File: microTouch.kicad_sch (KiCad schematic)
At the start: 9 parts, among them J1 SERVO, J2 PRINTER, U1 T1302

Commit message: smaller
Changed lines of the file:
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@@
   )
   (symbol (lib_id "Device:LED") (at 105.41 82.55 180) (unit 1)
-    (in_bom yes) (on_board yes) (fields_autoplaced)
-    (property "Reference" "D1" (id 0) (at 105.7909 76.4245 0))
-    (property "Value" "LED" (id 1) (at 105.7909 79.1996 0))
+    (in_bom yes) (on_board yes)
+    (property "Reference" "D1" (id 0) (at 105.7909 85.3145 0))
+    (property "Value" "LED" (id 1) (at 105.7909 88.0896 0))
     (property "Footprint" "LED_SMD:LED_0603_1608Metric_Pad1.05x0.95mm_HandSolder" (id 2) (at 105.41 82.55 0)
       (effects (font (size 1.27 1.27)) hide)

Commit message: assorted tweaks
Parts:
- D1: footprint LED_SMD:LED_0603_1608Metric_Pad1.05x0.95mm_HandSolder -> LED_SMD:LED_0805_2012Metric_Pad1.15x1.40mm_HandSolder
- R1, R2, R3: footprint Resistor_SMD:R_0603_1608Metric_Pad0.98x0.95mm_HandSolder -> Resistor_SMD:R_0805_2012Metric_Pad1.20x1.40mm_HandSolder
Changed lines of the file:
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@@
     (property "Reference" "R1" (id 0) (at 86.36 58.7969 90))
     (property "Value" "220" (id 1) (at 86.36 61.572 90))
-    (property "Footprint" "Resistor_SMD:R_0603_1608Metric_Pad0.98x0.95mm_HandSolder" (id 2) (at 86.36 63.5 0)
+    (property "Footprint" "Resistor_SMD:R_0805_2012Metric_Pad1.20x1.40mm_HandSolder" (id 2) (at 86.36 63.5 0)
       (effects (font (size 1.27 1.27)) hide)
     )
@@
     (property "Reference" "R2" (id 0) (at 105.41 68.9569 90))
     (property "Value" "1K" (id 1) (at 105.41 71.732 90))
-    (property "Footprint" "Resistor_SMD:R_0603_1608Metric_Pad0.98x0.95mm_HandSolder" (id 2) (at 105.41 73.66 0)
+    (property "Footprint" "Resistor_SMD:R_0805_2012Metric_Pad1.20x1.40mm_HandSolder" (id 2) (at 105.41 73.66 0)
       (effects (font (size 1.27 1.27)) hide)
     )
@@
     (property "Reference" "R3" (id 0) (at 114.3 77.8469 90))
     (property "Value" "2K2" (id 1) (at 114.3 80.622 90))
-    (property "Footprint" "Resistor_SMD:R_0603_1608Metric_Pad0.98x0.95mm_HandSolder" (id 2) (at 114.3 82.55 0)
+    (property "Footprint" "Resistor_SMD:R_0805_2012Metric_Pad1.20x1.40mm_HandSolder" (id 2) (at 114.3 82.55 0)
       (effects (font (size 1.27 1.27)) hide)
     )
@@
     (property "Reference" "D1" (id 0) (at 105.7909 85.3145 0))
     (property "Value" "LED" (id 1) (at 105.7909 88.0896 0))
-    (property "Footprint" "LED_SMD:LED_0603_1608Metric_Pad1.05x0.95mm_HandSolder" (id 2) (at 105.41 82.55 0)
+    (property "Footprint" "LED_SMD:LED_0805_2012Metric_Pad1.15x1.40mm_HandSolder" (id 2) (at 105.41 82.55 0)
       (effects (font (size 1.27 1.27)) hide)
     )
@@
     )
     (path "/7408d9bb-2040-4db4-9f32-e25e485fbe0e"
-      (reference "D1") (unit 1) (value "LED") (footprint "LED_SMD:LED_0603_1608Metric_Pad1.05x0.95mm_HandSolder")
+      (reference "D1") (unit 1) (value "LED") (footprint "LED_SMD:LED_0805_2012Metric_Pad1.15x1.40mm_HandSolder")
     )
     (path "/0c5ed85d-1f3f-4d6f-ab20-e65b16190c7b"
@@
     )
     (path "/addec1fb-b8e8-4fc7-8f03-f3f97a48f7fe"
-      (reference "R1") (unit 1) (value "220") (footprint "Resistor_SMD:R_0603_1608Metric_Pad0.98x0.95mm_HandSolder")
+      (reference "R1") (unit 1) (value "220") (footprint "Resistor_SMD:R_0805_2012Metric_Pad1.20x1.40mm_HandSolder")
     )
     (path "/d6cfadea-d8b7-4535-b6c3-a7d2fdbcf92b"
-      (reference "R2") (unit 1) (value "1K") (footprint "Resistor_SMD:R_0603_1608Metric_Pad0.98x0.95mm_HandSolder")
+      (reference "R2") (unit 1) (value "1K") (footprint "Resistor_SMD:R_0805_2012Metric_Pad1.20x1.40mm_HandSolder")
     )
     (path "/6ec2e99d-5757-45f7-89ab-e4a3e466c2e0"
-      (reference "R3") (unit 1) (value "2K2") (footprint "Resistor_SMD:R_0603_1608Metric_Pad0.98x0.95mm_HandSolder")
+      (reference "R3") (unit 1) (value "2K2") (footprint "Resistor_SMD:R_0805_2012Metric_Pad1.20x1.40mm_HandSolder")
     )
     (path "/a4631f7f-c98e-425f-863a-b5265e18ace0"

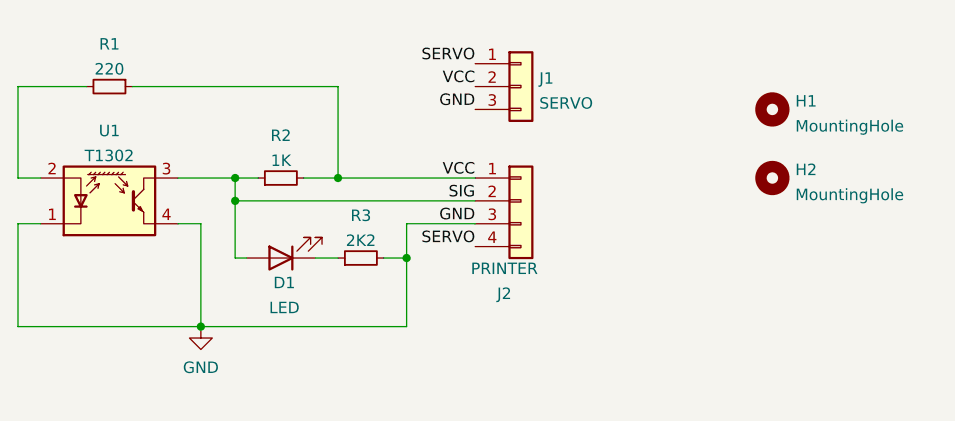
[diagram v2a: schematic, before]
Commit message: fix photint pinout, adjust pullup, move LED out further
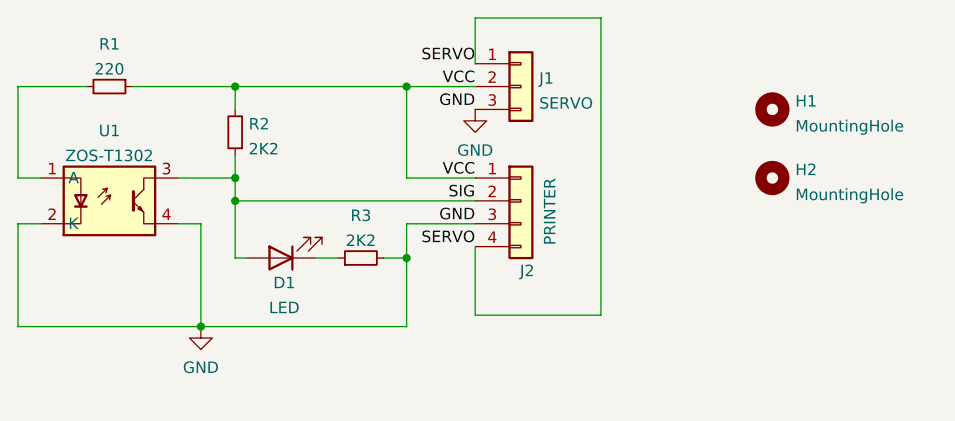
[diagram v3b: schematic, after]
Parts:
- removed U1: T1302, microTouch:T1302, symbol Sensor_Proximity:BPR-105F
- added U1: ZOS-T1302, microTouch:T1302, symbol microTouch:ZOS-T1302
- R2: value 1K -> 2K2
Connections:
- net GND: now also U1.2 (K), U1.4
- net SIG: now also U1.3
- net at R1.2: now also U1.1 (A)
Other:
- moved on the sheet: R2
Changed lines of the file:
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@@
   (paper "A4")
   (junction (at 96.52 90.17) (diameter 0) (color 0 0 0 0))
+  (junction (at 100.33 63.5) (diameter 0) (color 0 0 0 0))
   (junction (at 100.33 73.66) (diameter 0) (color 0 0 0 0))
   (junction (at 100.33 76.2) (diameter 0) (color 0 0 0 0))
-  (junction (at 111.76 73.66) (diameter 0) (color 0 0 0 0))
+  (junction (at 119.38 63.5) (diameter 0) (color 0 0 0 0))
   (junction (at 119.38 82.55) (diameter 0) (color 0 0 0 0))
   (wire (pts (xy 76.2 63.5) (xy 76.2 73.66))
@@
     (stroke (width 0) (type default) (color 0 0 0 0))
   )
-  (wire (pts (xy 88.9 63.5) (xy 111.76 63.5))
+  (wire (pts (xy 88.9 63.5) (xy 100.33 63.5))
     (stroke (width 0) (type default) (color 0 0 0 0))
   )
@@
     (stroke (width 0) (type default) (color 0 0 0 0))
   )
-  (wire (pts (xy 100.33 73.66) (xy 102.87 73.66))
+  (wire (pts (xy 100.33 63.5) (xy 100.33 66.04))
+    (stroke (width 0) (type default) (color 0 0 0 0))
+  )
+  (wire (pts (xy 100.33 63.5) (xy 119.38 63.5))
+    (stroke (width 0) (type default) (color 0 0 0 0))
+  )
+  (wire (pts (xy 100.33 71.12) (xy 100.33 73.66))
     (stroke (width 0) (type default) (color 0 0 0 0))
   )
@@
     (stroke (width 0) (type default) (color 0 0 0 0))
   )
-  (wire (pts (xy 107.95 73.66) (xy 111.76 73.66))
-    (stroke (width 0) (type default) (color 0 0 0 0))
-  )
   (wire (pts (xy 109.22 82.55) (xy 111.76 82.55))
     (stroke (width 0) (type default) (color 0 0 0 0))
   )
-  (wire (pts (xy 111.76 63.5) (xy 111.76 73.66))
-    (stroke (width 0) (type default) (color 0 0 0 0))
-  )
-  (wire (pts (xy 111.76 73.66) (xy 127 73.66))
-    (stroke (width 0) (type default) (color 0 0 0 0))
-  )
   (wire (pts (xy 116.84 82.55) (xy 119.38 82.55))
     (stroke (width 0) (type default) (color 0 0 0 0))
   )
+  (wire (pts (xy 119.38 63.5) (xy 127 63.5))
+    (stroke (width 0) (type default) (color 0 0 0 0))
+  )
+  (wire (pts (xy 119.38 73.66) (xy 119.38 63.5))
+    (stroke (width 0) (type default) (color 0 0 0 0))
+  )
   (wire (pts (xy 119.38 78.74) (xy 127 78.74))
     (stroke (width 0) (type default) (color 0 0 0 0))
@@
     (stroke (width 0) (type default) (color 0 0 0 0))
   )
+  (wire (pts (xy 127 55.88) (xy 140.97 55.88))
+    (stroke (width 0) (type default) (color 0 0 0 0))
+  )
+  (wire (pts (xy 127 60.96) (xy 127 55.88))
+    (stroke (width 0) (type default) (color 0 0 0 0))
+  )
+  (wire (pts (xy 127 73.66) (xy 119.38 73.66))
+    (stroke (width 0) (type default) (color 0 0 0 0))
+  )
   (wire (pts (xy 127 76.2) (xy 100.33 76.2))
+    (stroke (width 0) (type default) (color 0 0 0 0))
+  )
+  (wire (pts (xy 127 88.9) (xy 127 81.28))
+    (stroke (width 0) (type default) (color 0 0 0 0))
+  )
+  (wire (pts (xy 140.97 55.88) (xy 140.97 88.9))
+    (stroke (width 0) (type default) (color 0 0 0 0))
+  )
+  (wire (pts (xy 140.97 88.9) (xy 127 88.9))
     (stroke (width 0) (type default) (color 0 0 0 0))
   )
@@
     )
     (property "Datasheet" "" (id 3) (at 96.52 90.17 0)
+      (effects (font (size 1.27 1.27)) hide)
+    )
+    (pin "1")
+  )
+  (symbol (lib_id "power:GND") (at 127 66.04 0) (unit 1)
+    (in_bom yes) (on_board yes) (fields_autoplaced)
+    (property "Reference" "#PWR?" (id 0) (at 127 72.39 0)
+      (effects (font (size 1.27 1.27)) hide)
+    )
+    (property "Value" "GND" (id 1) (at 127 70.6024 0))
+    (property "Footprint" "" (id 2) (at 127 66.04 0)
+      (effects (font (size 1.27 1.27)) hide)
+    )
+    (property "Datasheet" "" (id 3) (at 127 66.04 0)
       (effects (font (size 1.27 1.27)) hide)
     )
@@
     (pin "2")
   )
-  (symbol (lib_id "Device:R_Small") (at 105.41 73.66 90) (unit 1)
-    (in_bom yes) (on_board yes) (fields_autoplaced)
-    (property "Reference" "R2" (id 0) (at 105.41 68.9569 90))
-    (property "Value" "1K" (id 1) (at 105.41 71.732 90))
-    (property "Footprint" "Resistor_SMD:R_0805_2012Metric_Pad1.20x1.40mm_HandSolder" (id 2) (at 105.41 73.66 0)
-      (effects (font (size 1.27 1.27)) hide)
-    )
-    (property "Datasheet" "~" (id 3) (at 105.41 73.66 0)
+  (symbol (lib_id "Device:R_Small") (at 100.33 68.58 180) (unit 1)
+    (in_bom yes) (on_board yes) (fields_autoplaced)
+    (property "Reference" "R2" (id 0) (at 101.8286 67.6715 0)
+      (effects (font (size 1.27 1.27)) (justify right))
+    )
+    (property "Value" "2K2" (id 1) (at 101.8286 70.4466 0)
+      (effects (font (size 1.27 1.27)) (justify right))
+    )
+    (property "Footprint" "Resistor_SMD:R_0805_2012Metric_Pad1.20x1.40mm_HandSolder" (id 2) (at 100.33 68.58 0)
+      (effects (font (size 1.27 1.27)) hide)
+    )
+    (property "Datasheet" "~" (id 3) (at 100.33 68.58 0)
       (effects (font (size 1.27 1.27)) hide)
     )
@@
   )
   (symbol (lib_id "Connector_Generic:Conn_01x04") (at 132.08 76.2 0) (unit 1)
-    (in_bom yes) (on_board yes) (fields_autoplaced)
-    (property "Reference" "J2" (id 0) (at 130.2385 86.5165 0))
-    (property "Value" "PRINTER" (id 1) (at 130.2385 83.7414 0))
+    (in_bom yes) (on_board yes)
+    (property "Reference" "J2" (id 0) (at 132.7785 83.9765 0))
+    (property "Value" "PRINTER" (id 1) (at 135.3185 77.3914 90))
     (property "Footprint" "Connector_JST:JST_PH_B4B-PH-K_1x04_P2.00mm_Vertical" (id 2) (at 132.08 76.2 0)
       (effects (font (size 1.27 1.27)) hide)
@@
     (pin "4")
   )
-  (symbol (lib_id "Sensor_Proximity:BPR-105F") (at 86.36 76.2 0) (unit 1)
+  (symbol (lib_id "microTouch:ZOS-T1302") (at 86.36 76.2 0) (unit 1)
     (in_bom yes) (on_board yes) (fields_autoplaced)
     (property "Reference" "U1" (id 0) (at 86.36 68.4235 0))
-    (property "Value" "T1302" (id 1) (at 86.36 71.1986 0))
-    (property "Footprint" "microTouch:T1302" (id 2) (at 86.36 81.28 0)
-      (effects (font (size 1.27 1.27)) hide)
-    )
-    (property "Datasheet" "http://www.ystone.com.tw/en/data/goods/IRPT/Photo%20Interrupters-Reflective%20Type.pdf" (id 3) (at 86.36 73.66 0)
+    (property "Value" "ZOS-T1302" (id 1) (at 86.36 71.1986 0))
+    (property "Footprint" "microTouch:T1302" (id 2) (at 86.36 76.2 0)
+      (effects (font (size 1.27 1.27)) hide)
+    )
+    (property "Datasheet" "" (id 3) (at 86.36 76.2 0)
       (effects (font (size 1.27 1.27)) hide)
     )
@@
       (reference "#PWR01") (unit 1) (value "GND") (footprint "")
     )
+    (path "/615251e4-00d3-4694-93b4-edb937059fda"
+      (reference "#PWR?") (unit 1) (value "GND") (footprint "")
+    )
     (path "/7408d9bb-2040-4db4-9f32-e25e485fbe0e"
       (reference "D1") (unit 1) (value "LED") (footprint "LED_SMD:LED_0805_2012Metric_Pad1.15x1.40mm_HandSolder")
@@
     )
     (path "/d6cfadea-d8b7-4535-b6c3-a7d2fdbcf92b"
-      (reference "R2") (unit 1) (value "1K") (footprint "Resistor_SMD:R_0805_2012Metric_Pad1.20x1.40mm_HandSolder")
+      (reference "R2") (unit 1) (value "2K2") (footprint "Resistor_SMD:R_0805_2012Metric_Pad1.20x1.40mm_HandSolder")
     )
     (path "/6ec2e99d-5757-45f7-89ab-e4a3e466c2e0"
       (reference "R3") (unit 1) (value "2K2") (footprint "Resistor_SMD:R_0805_2012Metric_Pad1.20x1.40mm_HandSolder")
     )
-    (path "/a4631f7f-c98e-425f-863a-b5265e18ace0"
-      (reference "U1") (unit 1) (value "T1302") (footprint "microTouch:T1302")
-    )
-  )
+    (path "/5c366571-0b2a-4b91-b149-dcee62dd11ce"
+      (reference "U1") (unit 1) (value "ZOS-T1302") (footprint "microTouch:T1302")
+    )
+  )

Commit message: redesign with a A3144 hall effect sensor
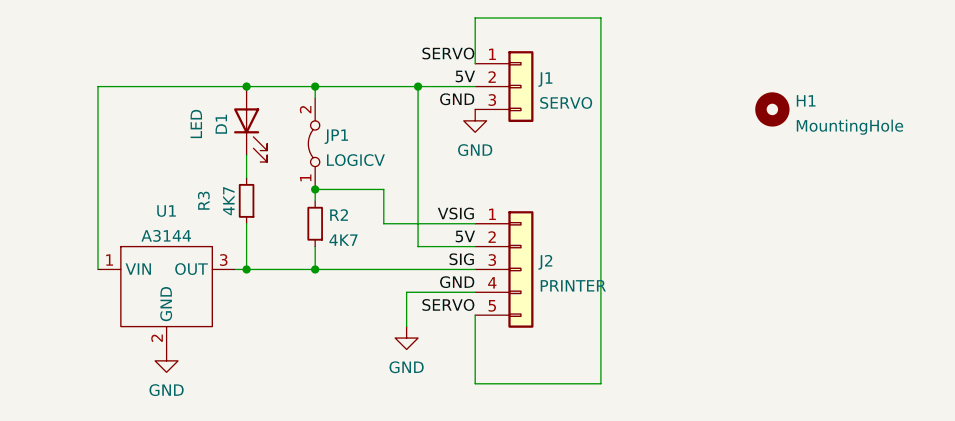
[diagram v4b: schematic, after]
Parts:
- removed H2: MountingHole, MountingHole:MountingHole_3.2mm_M3, symbol Mechanical:MountingHole
- removed J2: PRINTER, Connector_JST:JST_PH_B4B-PH-K_1x04_P2.00mm_Vertical, symbol Connector_Generic:Conn_01x04
- removed R1: 220, Resistor_SMD:R_0805_2012Metric_Pad1.20x1.40mm_HandSolder, symbol Device:R_Small
- removed U1: ZOS-T1302, microTouch:T1302, symbol microTouch:ZOS-T1302
- added J2: PRINTER, Connector_JST:JST_PH_B5B-PH-K_1x05_P2.00mm_Vertical, symbol Connector_Generic:Conn_01x05
- added JP1: LOGICV, Jumper:SolderJumper-2_P1.3mm_Bridged_RoundedPad1.0x1.5mm, symbol Jumper:Jumper_2_Bridged
- added U1: A3144, Package_TO_SOT_THT:TO-92Flat, symbol microTouch:A3144
- R2, R3: value 2K2 -> 4K7
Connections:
- net GND: now also J2.4 (Pin_4), U1.2 (GND); no longer R3.2
- net SERVO: now also J2.5 (Pin_5)
- net SIG: now also R3.1, J2.3 (Pin_3), U1.3 (OUT); no longer D1.2 (A)
- net at D1.1 (K): now also R3.2; no longer R3.1
- net VCC renamed 5V
- net 5V: now also D1.2 (A), J2.2 (Pin_2), JP1.2 (B), U1.1 (VIN); no longer R2.2
- new net VSIG: J2.1 (Pin_1), JP1.1 (A), R2.2
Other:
- moved on the sheet: D1, R2, R3

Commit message: move some stuff around, add some filter caps for noise
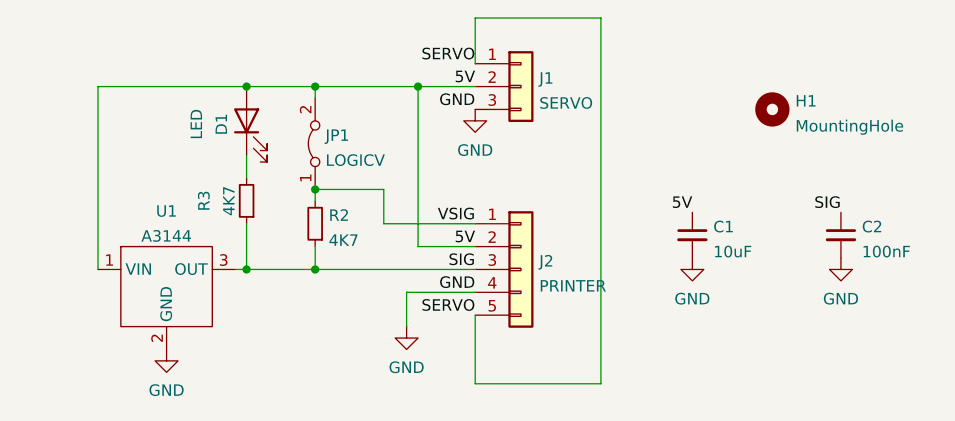
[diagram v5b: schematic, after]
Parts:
- added C1: 10uF, Capacitor_SMD:C_0805_2012Metric_Pad1.18x1.45mm_HandSolder, symbol Device:C_Small
- added C2: 100nF, Capacitor_SMD:C_0805_2012Metric_Pad1.18x1.45mm_HandSolder, symbol Device:C_Small
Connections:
- net 5V: now also C1.1
- net GND: now also C1.2, C2.2
- net SIG: now also C2.1
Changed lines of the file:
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@@
+    (effects (font (size 1.27 1.27)) (justify right bottom))
+  )
+  (label "5V" (at 151.13 77.47 180)
+    (effects (font (size 1.27 1.27)) (justify right bottom))
+  )
+  (label "SIG" (at 167.64 77.47 180)
     (effects (font (size 1.27 1.27)) (justify right bottom))
   )
@@
     )
     (property "Datasheet" "" (id 3) (at 127 66.04 0)
+      (effects (font (size 1.27 1.27)) hide)
+    )
+    (pin "1")
+  )
+  (symbol (lib_id "power:GND") (at 151.13 82.55 0) (unit 1)
+    (in_bom yes) (on_board yes) (fields_autoplaced)
+    (property "Reference" "#PWR0103" (id 0) (at 151.13 88.9 0)
+      (effects (font (size 1.27 1.27)) hide)
+    )
+    (property "Value" "GND" (id 1) (at 151.13 87.1124 0))
+    (property "Footprint" "" (id 2) (at 151.13 82.55 0)
+      (effects (font (size 1.27 1.27)) hide)
+    )
+    (property "Datasheet" "" (id 3) (at 151.13 82.55 0)
+      (effects (font (size 1.27 1.27)) hide)
+    )
+    (pin "1")
+  )
+  (symbol (lib_id "power:GND") (at 167.64 82.55 0) (unit 1)
+    (in_bom yes) (on_board yes) (fields_autoplaced)
+    (property "Reference" "#PWR0104" (id 0) (at 167.64 88.9 0)
+      (effects (font (size 1.27 1.27)) hide)
+    )
+    (property "Value" "GND" (id 1) (at 167.64 87.1124 0))
+    (property "Footprint" "" (id 2) (at 167.64 82.55 0)
+      (effects (font (size 1.27 1.27)) hide)
+    )
+    (property "Datasheet" "" (id 3) (at 167.64 82.55 0)
       (effects (font (size 1.27 1.27)) hide)
     )
@@
     )
   )
+  (symbol (lib_id "Device:C_Small") (at 151.13 80.01 0) (unit 1)
+    (in_bom yes) (on_board yes) (fields_autoplaced)
+    (property "Reference" "C1" (id 0) (at 153.4541 79.1015 0)
+      (effects (font (size 1.27 1.27)) (justify left))
+    )
+    (property "Value" "10uF" (id 1) (at 153.4541 81.8766 0)
+      (effects (font (size 1.27 1.27)) (justify left))
+    )
+    (property "Footprint" "Capacitor_SMD:C_0805_2012Metric_Pad1.18x1.45mm_HandSolder" (id 2) (at 151.13 80.01 0)
+      (effects (font (size 1.27 1.27)) hide)
+    )
+    (property "Datasheet" "~" (id 3) (at 151.13 80.01 0)
+      (effects (font (size 1.27 1.27)) hide)
+    )
+    (pin "1")
+    (pin "2")
+  )
+  (symbol (lib_id "Device:C_Small") (at 167.64 80.01 0) (unit 1)
+    (in_bom yes) (on_board yes) (fields_autoplaced)
+    (property "Reference" "C2" (id 0) (at 169.9641 79.1015 0)
+      (effects (font (size 1.27 1.27)) (justify left))
+    )
+    (property "Value" "100nF" (id 1) (at 169.9641 81.8766 0)
+      (effects (font (size 1.27 1.27)) (justify left))
+    )
+    (property "Footprint" "Capacitor_SMD:C_0805_2012Metric_Pad1.18x1.45mm_HandSolder" (id 2) (at 167.64 80.01 0)
+      (effects (font (size 1.27 1.27)) hide)
+    )
+    (property "Datasheet" "~" (id 3) (at 167.64 80.01 0)
+      (effects (font (size 1.27 1.27)) hide)
+    )
+    (pin "1")
+    (pin "2")
+  )
   (symbol (lib_id "Device:LED") (at 101.6 67.31 90) (unit 1)
     (in_bom yes) (on_board yes)
@@
       (reference "#PWR0102") (unit 1) (value "GND") (footprint "")
     )
+    (path "/6555b08e-39a8-47c6-a87d-4e25391810cd"
+      (reference "#PWR0103") (unit 1) (value "GND") (footprint "")
+    )
+    (path "/ddc2e6c1-5619-4236-98b9-1579d6d8438d"
+      (reference "#PWR0104") (unit 1) (value "GND") (footprint "")
+    )
+    (path "/1eb53274-0914-4a8b-9bc2-33d82143e9e3"
+      (reference "C1") (unit 1) (value "10uF") (footprint "Capacitor_SMD:C_0805_2012Metric_Pad1.18x1.45mm_HandSolder")
+    )
+    (path "/b377ce04-7e74-4f2a-af9f-ec1a16d1bac7"
+      (reference "C2") (unit 1) (value "100nF") (footprint "Capacitor_SMD:C_0805_2012Metric_Pad1.18x1.45mm_HandSolder")
+    )
     (path "/7408d9bb-2040-4db4-9f32-e25e485fbe0e"

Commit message: a few more layout tweaks
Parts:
- U1: footprint Package_TO_SOT_THT:TO-92Flat -> microTouch:TO-92Flat_Oval
